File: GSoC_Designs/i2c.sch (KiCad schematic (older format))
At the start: 3 parts

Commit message: Fixed some ERC Errors
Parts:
- gave numbers to parts that had none: 3
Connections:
- net GND: now also U6.4 (GND), U7.4 (GND)
- net OVDD: now also U6.1 (VCCA), U7.1 (VCCA)
- net SCL_VGA_RX: now also U6.7 (SCLB)
- net SCL_VGA_RX_BUF: now also U6.2 (SCLA)
- net SCL_VGA_TX: now also U7.7 (SCLB)
- net SCL_VGA_TX_BUF: now also U7.2 (SCLA)
- net SDA_VGA_RX: now also U6.6 (SDAB)
- net SDA_VGA_RX_BUF: now also U6.3 (SDAA)
- net SDA_VGA_TX: now also U7.6 (SDAB)
- net SDA_VGA_TX_BUF: now also U7.3 (SDAA)
- net VCC: now also U7.8 (VCCB)
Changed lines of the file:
@@
 SDA_VGA_TX_BUF
 $Comp
-L 24AA014 U?
+L 24AA014 U5
 U 1 1 53BEC2F7
 P 8550 3400
-F 0 "U?" H 8700 3750 60  0000 C CNN
+F 0 "U5" H 8700 3750 60  0000 C CNN
 F 1 "24AA014" H 8750 3050 60  0000 C CNN
 F 2 "~" H 8550 3400 60  0000 C CNN
@@
 	1    0    0    -1
 $EndComp
-Wire Wire Line
-	9250 3200 9450 3200
-Wire Wire Line
-	9250 3300 9450 3300
-Wire Wire Line
-	8550 2550 8550 2900
-Wire Wire Line
-	8550 3900 8550 4200
-Wire Wire Line
-	7850 3600 7850 4050
-Wire Wire Line
-	7850 4050 8550 4050
-Connection ~ 8550 4050
 $Comp
-L TCA9617A U?
+L TCA9617A U6
 U 1 1 53BEC835
 P 3900 4450
-F 0 "U?" H 3900 4400 60  0000 C CNN
+F 0 "U6" H 3900 4400 60  0000 C CNN
 F 1 "TCA9617A" H 3900 4500 60  0000 C CNN
 F 2 "" H 4150 4550 60  0000 C CNN
@@
 $EndComp
 $Comp
-L TCA9617A U?
+L TCA9617A U7
 U 1 1 53BEC842
 P 3900 5350
-F 0 "U?" H 3900 5300 60  0000 C CNN
+F 0 "U7" H 3900 5300 60  0000 C CNN
 F 1 "TCA9617A" H 3900 5400 60  0000 C CNN
 F 2 "" H 4150 5450 60  0000 C CNN
@@
 NoConn ~ 4700 5550
 NoConn ~ 4700 4650
+Wire Wire Line
+	9250 3200 9450 3200
+Wire Wire Line
+	9250 3300 9450 3300
+Wire Wire Line
+	8550 2550 8550 2900
+Wire Wire Line
+	8550 3900 8550 4050
+Wire Wire Line
+	8550 4050 8550 4200
+Wire Wire Line
+	7850 3600 7850 4050
+Wire Wire Line
+	7850 4050 8550 4050
+Connection ~ 8550 4050
+Wire Wire Line
+	2900 4200 3100 4200
+Wire Wire Line
+	2900 4350 3100 4350
+Wire Wire Line
+	2900 4500 3100 4500
+Wire Wire Line
+	2900 4650 3100 4650
+Wire Wire Line
+	2900 5100 3100 5100
+Wire Wire Line
+	2900 5250 3100 5250
+Wire Wire Line
+	2900 5400 3100 5400
+Wire Wire Line
+	2900 5550 3100 5550
+Wire Wire Line
+	4700 4350 4900 4350
+Wire Wire Line
+	4700 4500 4900 4500
+Wire Wire Line
+	4700 5100 4900 5100
+Wire Wire Line
+	4700 5250 4900 5250
+Wire Wire Line
+	4700 5400 4900 5400
 $EndSCHEMATC

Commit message: All ERC Errors fixed
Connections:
- net GND: now also U5.3 (A2)
- net OVDD: now also U5.1 (A0), U5.2 (A1)
- net VCC: now also U6.8 (VCCB)
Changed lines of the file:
@@
 Text HLabel 2900 4350 0    60   BiDi ~ 0
 SCL_VGA_RX_BUF
-Text HLabel 2900 4500 0    60   BiDi ~ 0
+Text HLabel 2850 4500 0    60   BiDi ~ 0
 SDA_VGA_RX_BUF
 Text HLabel 2900 5250 0    60   BiDi ~ 0
@@
 	8550 2550 8550 2900
 Wire Wire Line
-	8550 3900 8550 4050
-Wire Wire Line
-	8550 4050 8550 4200
+	8550 3900 8550 4200
 Wire Wire Line
 	7850 3600 7850 4050
@@
 Wire Wire Line
 	2900 4350 3100 4350
-Wire Wire Line
-	2900 4500 3100 4500
 Wire Wire Line
 	2900 4650 3100 4650
@@
 Wire Wire Line
 	4700 5400 4900 5400
+Text HLabel 4900 4200 2    60   Input ~ 0
+VCC
+Wire Wire Line
+	4900 4200 4700 4200
+Text HLabel 7600 3200 0    60   Input ~ 0
+OVDD
+Text HLabel 7600 3300 0    60   Input ~ 0
+OVDD
+Text HLabel 7600 3400 0    60   Input ~ 0
+GND
+Wire Wire Line
+	7600 3200 7850 3200
+Wire Wire Line
+	7600 3300 7850 3300
+Wire Wire Line
+	7600 3400 7850 3400
+Wire Wire Line
+	3100 4500 2850 4500
 $EndSCHEMATC

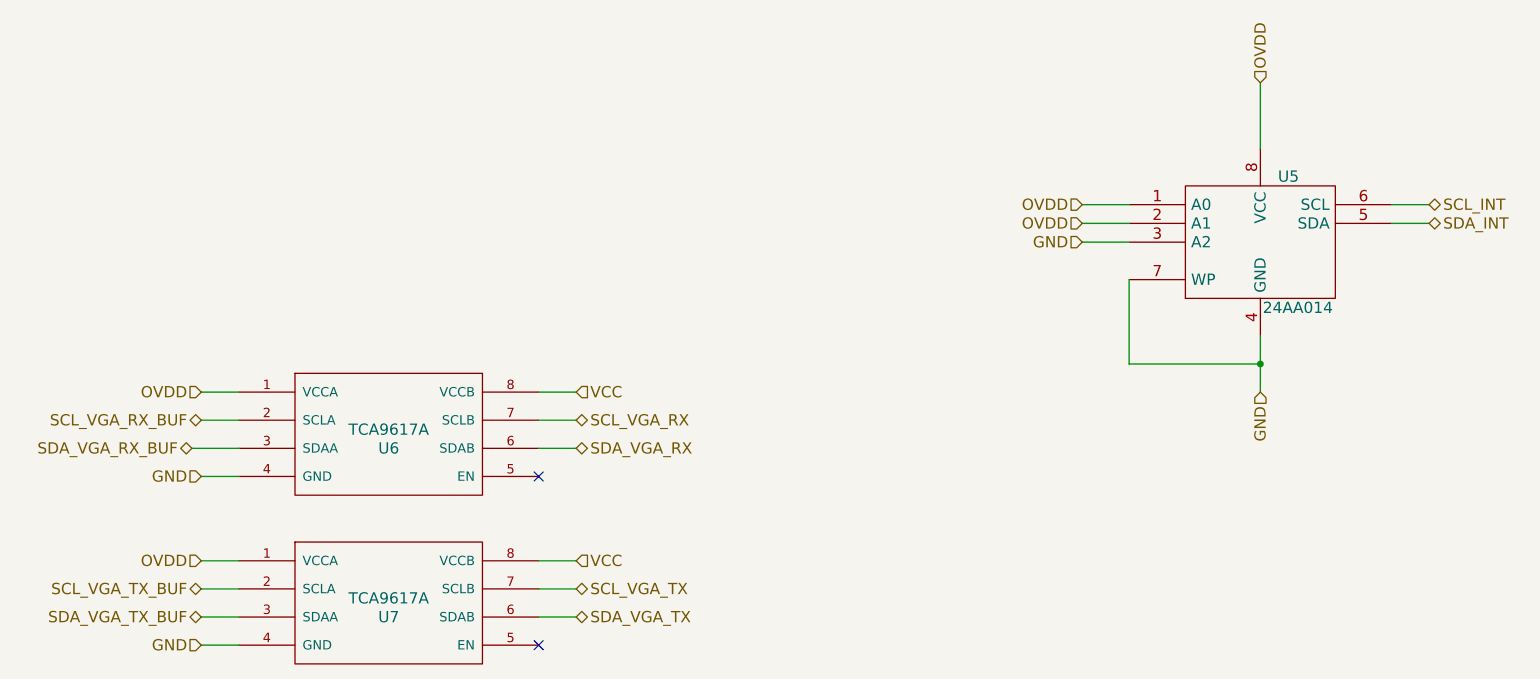
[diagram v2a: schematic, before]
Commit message: Added TestPoints
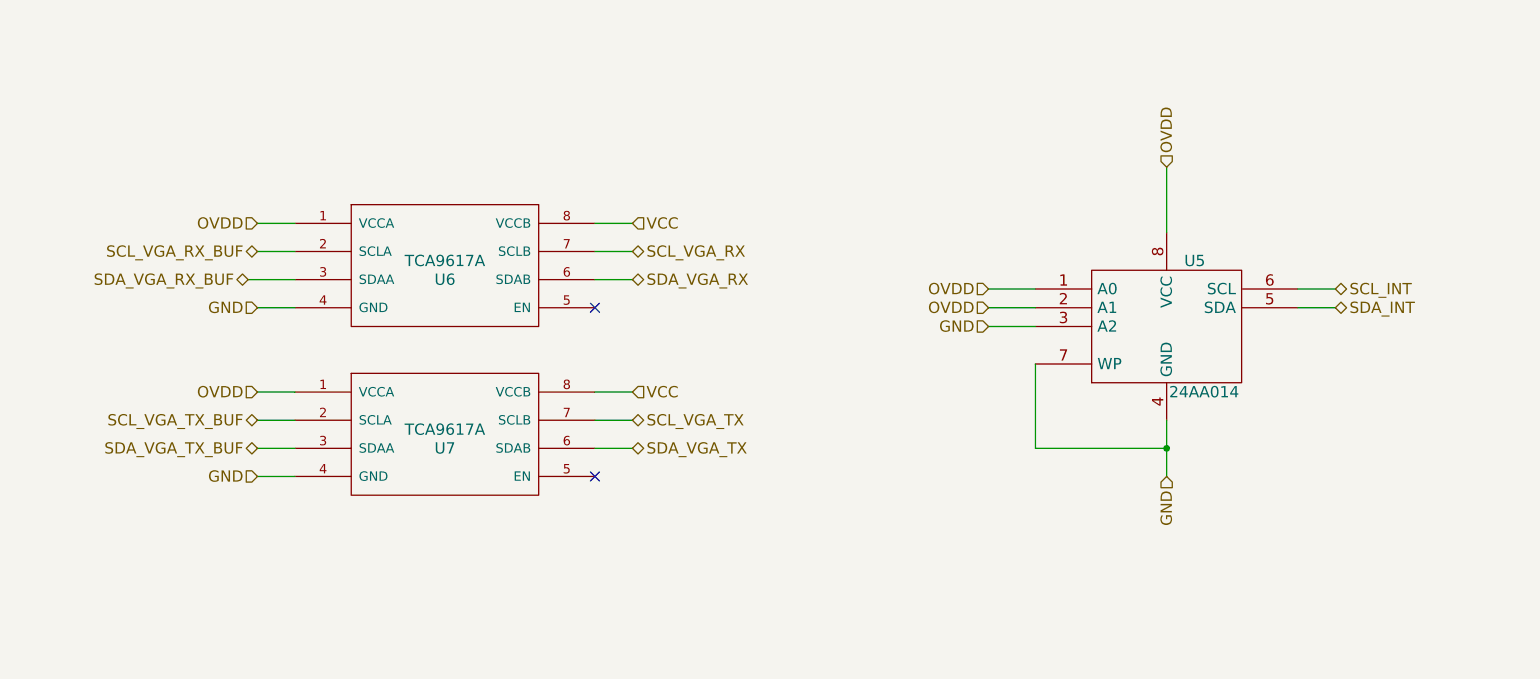
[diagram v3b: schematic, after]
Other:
- moved on the sheet: U5, U6, U7
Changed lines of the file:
@@
 LIBS:24AA014
 LIBS:vmodvga
+LIBS:testpoint
 LIBS:vgaExp-cache
 EELAYER 27 0
@@
 Sheet 3 3
 Title ""
-Date "10 jul 2014"
+Date "11 jul 2014"
 Rev ""
 Comp ""
@@
 Comment4 ""
 $EndDescr
-Text HLabel 4900 4350 2    60   BiDi ~ 0
+Text HLabel 5200 3450 2    60   BiDi ~ 0
 SCL_VGA_RX
-Text HLabel 4900 4500 2    60   BiDi ~ 0
+Text HLabel 5200 3600 2    60   BiDi ~ 0
 SDA_VGA_RX
-Text HLabel 4900 5250 2    60   BiDi ~ 0
+Text HLabel 5200 4350 2    60   BiDi ~ 0
 SCL_VGA_TX
-Text HLabel 4900 5400 2    60   BiDi ~ 0
+Text HLabel 5200 4500 2    60   BiDi ~ 0
 SDA_VGA_TX
-Text HLabel 9450 3200 2    60   BiDi ~ 0
+Text HLabel 8950 3650 2    60   BiDi ~ 0
 SCL_INT
-Text HLabel 9450 3300 2    60   BiDi ~ 0
+Text HLabel 8950 3750 2    60   BiDi ~ 0
 SDA_INT
-Text HLabel 4900 5100 2    60   Input ~ 0
+Text HLabel 5200 4200 2    60   Input ~ 0
 VCC
-Text HLabel 8550 2550 1    60   Input ~ 0
+Text HLabel 8050 3000 1    60   Input ~ 0
 OVDD
-Text HLabel 8550 4200 3    60   Input ~ 0
+Text HLabel 8050 4650 3    60   Input ~ 0
 GND
-Text HLabel 2900 4350 0    60   BiDi ~ 0
+Text HLabel 3200 3450 0    60   BiDi ~ 0
 SCL_VGA_RX_BUF
-Text HLabel 2850 4500 0    60   BiDi ~ 0
+Text HLabel 3150 3600 0    60   BiDi ~ 0
 SDA_VGA_RX_BUF
-Text HLabel 2900 5250 0    60   BiDi ~ 0
+Text HLabel 3200 4350 0    60   BiDi ~ 0
 SCL_VGA_TX_BUF
-Text HLabel 2900 5400 0    60   BiDi ~ 0
+Text HLabel 3200 4500 0    60   BiDi ~ 0
 SDA_VGA_TX_BUF
 $Comp
 L 24AA014 U5
 U 1 1 53BEC2F7
-P 8550 3400
-F 0 "U5" H 8700 3750 60  0000 C CNN
-F 1 "24AA014" H 8750 3050 60  0000 C CNN
-F 2 "~" H 8550 3400 60  0000 C CNN
-F 3 "~" H 8550 3400 60  0000 C CNN
-	1    8550 3400
+P 8050 3850
+F 0 "U5" H 8200 4200 60  0000 C CNN
+F 1 "24AA014" H 8250 3500 60  0000 C CNN
+F 2 "~" H 8050 3850 60  0000 C CNN
+F 3 "~" H 8050 3850 60  0000 C CNN
+	1    8050 3850
 	1    0    0    -1
 $EndComp
@@
 L TCA9617A U6
 U 1 1 53BEC835
-P 3900 4450
-F 0 "U6" H 3900 4400 60  0000 C CNN
-F 1 "TCA9617A" H 3900 4500 60  0000 C CNN
-F 2 "" H 4150 4550 60  0000 C CNN
-F 3 "" H 4150 4550 60  0000 C CNN
-	1    3900 4450
+P 4200 3550
+F 0 "U6" H 4200 3500 60  0000 C CNN
+F 1 "TCA9617A" H 4200 3600 60  0000 C CNN
+F 2 "" H 4450 3650 60  0000 C CNN
+F 3 "" H 4450 3650 60  0000 C CNN
+	1    4200 3550
 	1    0    0    -1
 $EndComp
@@
 L TCA9617A U7
 U 1 1 53BEC842
-P 3900 5350
-F 0 "U7" H 3900 5300 60  0000 C CNN
-F 1 "TCA9617A" H 3900 5400 60  0000 C CNN
-F 2 "" H 4150 5450 60  0000 C CNN
-F 3 "" H 4150 5450 60  0000 C CNN
-	1    3900 5350
+P 4200 4450
+F 0 "U7" H 4200 4400 60  0000 C CNN
+F 1 "TCA9617A" H 4200 4500 60  0000 C CNN
+F 2 "" H 4450 4550 60  0000 C CNN
+F 3 "" H 4450 4550 60  0000 C CNN
+	1    4200 4450
 	1    0    0    -1
 $EndComp
-Text HLabel 2900 4200 0    60   Input ~ 0
+Text HLabel 3200 3300 0    60   Input ~ 0
 OVDD
-Text HLabel 2900 5100 0    60   Input ~ 0
+Text HLabel 3200 4200 0    60   Input ~ 0
 OVDD
-Text HLabel 2900 5550 0    60   Input ~ 0
+Text HLabel 3200 4650 0    60   Input ~ 0
 GND
-Text HLabel 2900 4650 0    60   Input ~ 0
+Text HLabel 3200 3750 0    60   Input ~ 0
 GND
-NoConn ~ 4700 5550
-NoConn ~ 4700 4650
+NoConn ~ 5000 4650
+NoConn ~ 5000 3750
 Wire Wire Line
-	9250 3200 9450 3200
+	8750 3650 8950 3650
 Wire Wire Line
-	9250 3300 9450 3300
+	8750 3750 8950 3750
 Wire Wire Line
-	8550 2550 8550 2900
+	8050 3000 8050 3350
 Wire Wire Line
-	8550 3900 8550 4200
+	8050 4350 8050 4650
 Wire Wire Line
-	7850 3600 7850 4050
+	7350 4050 7350 4500
 Wire Wire Line
-	7850 4050 8550 4050
-Connection ~ 8550 4050
+	7350 4500 8050 4500
+Connection ~ 8050 4500
 Wire Wire Line
-	2900 4200 3100 4200
+	3200 3300 3400 3300
 Wire Wire Line
-	2900 4350 3100 4350
+	3200 3450 3400 3450
 Wire Wire Line
-	2900 4650 3100 4650
+	3200 3750 3400 3750
 Wire Wire Line
-	2900 5100 3100 5100
+	3200 4200 3400 4200
 Wire Wire Line
-	2900 5250 3100 5250
+	3200 4350 3400 4350
 Wire Wire Line
-	2900 5400 3100 5400
+	3200 4500 3400 4500
 Wire Wire Line
-	2900 5550 3100 5550
+	3200 4650 3400 4650
 Wire Wire Line
-	4700 4350 4900 4350
+	5000 3450 5200 3450
 Wire Wire Line
-	4700 4500 4900 4500
+	5000 3600 5200 3600
 Wire Wire Line
-	4700 5100 4900 5100
+	5000 4200 5200 4200
 Wire Wire Line
-	4700 5250 4900 5250
+	5000 4350 5200 4350
 Wire Wire Line
-	4700 5400 4900 5400
-Text HLabel 4900 4200 2    60   Input ~ 0
+	5000 4500 5200 4500
+Text HLabel 5200 3300 2    60   Input ~ 0
 VCC
 Wire Wire Line
-	4900 4200 4700 4200
-Text HLabel 7600 3200 0    60   Input ~ 0
+	5200 3300 5000 3300
+Text HLabel 7100 3650 0    60   Input ~ 0
 OVDD
-Text HLabel 7600 3300 0    60   Input ~ 0
+Text HLabel 7100 3750 0    60   Input ~ 0
 OVDD
-Text HLabel 7600 3400 0    60   Input ~ 0
+Text HLabel 7100 3850 0    60   Input ~ 0
 GND
 Wire Wire Line
-	7600 3200 7850 3200
+	7100 3650 7350 3650
 Wire Wire Line
-	7600 3300 7850 3300
+	7100 3750 7350 3750
 Wire Wire Line
-	7600 3400 7850 3400
+	7100 3850 7350 3850
 Wire Wire Line
-	3100 4500 2850 4500
+	3400 3600 3150 3600
 $EndSCHEMATC
